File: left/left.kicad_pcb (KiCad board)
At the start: 2 copper layers, 173.8 x 173.8 mm, 67 parts, among them J1 HDMI_C_1.4, U1 Raspberry_Pi_Pico

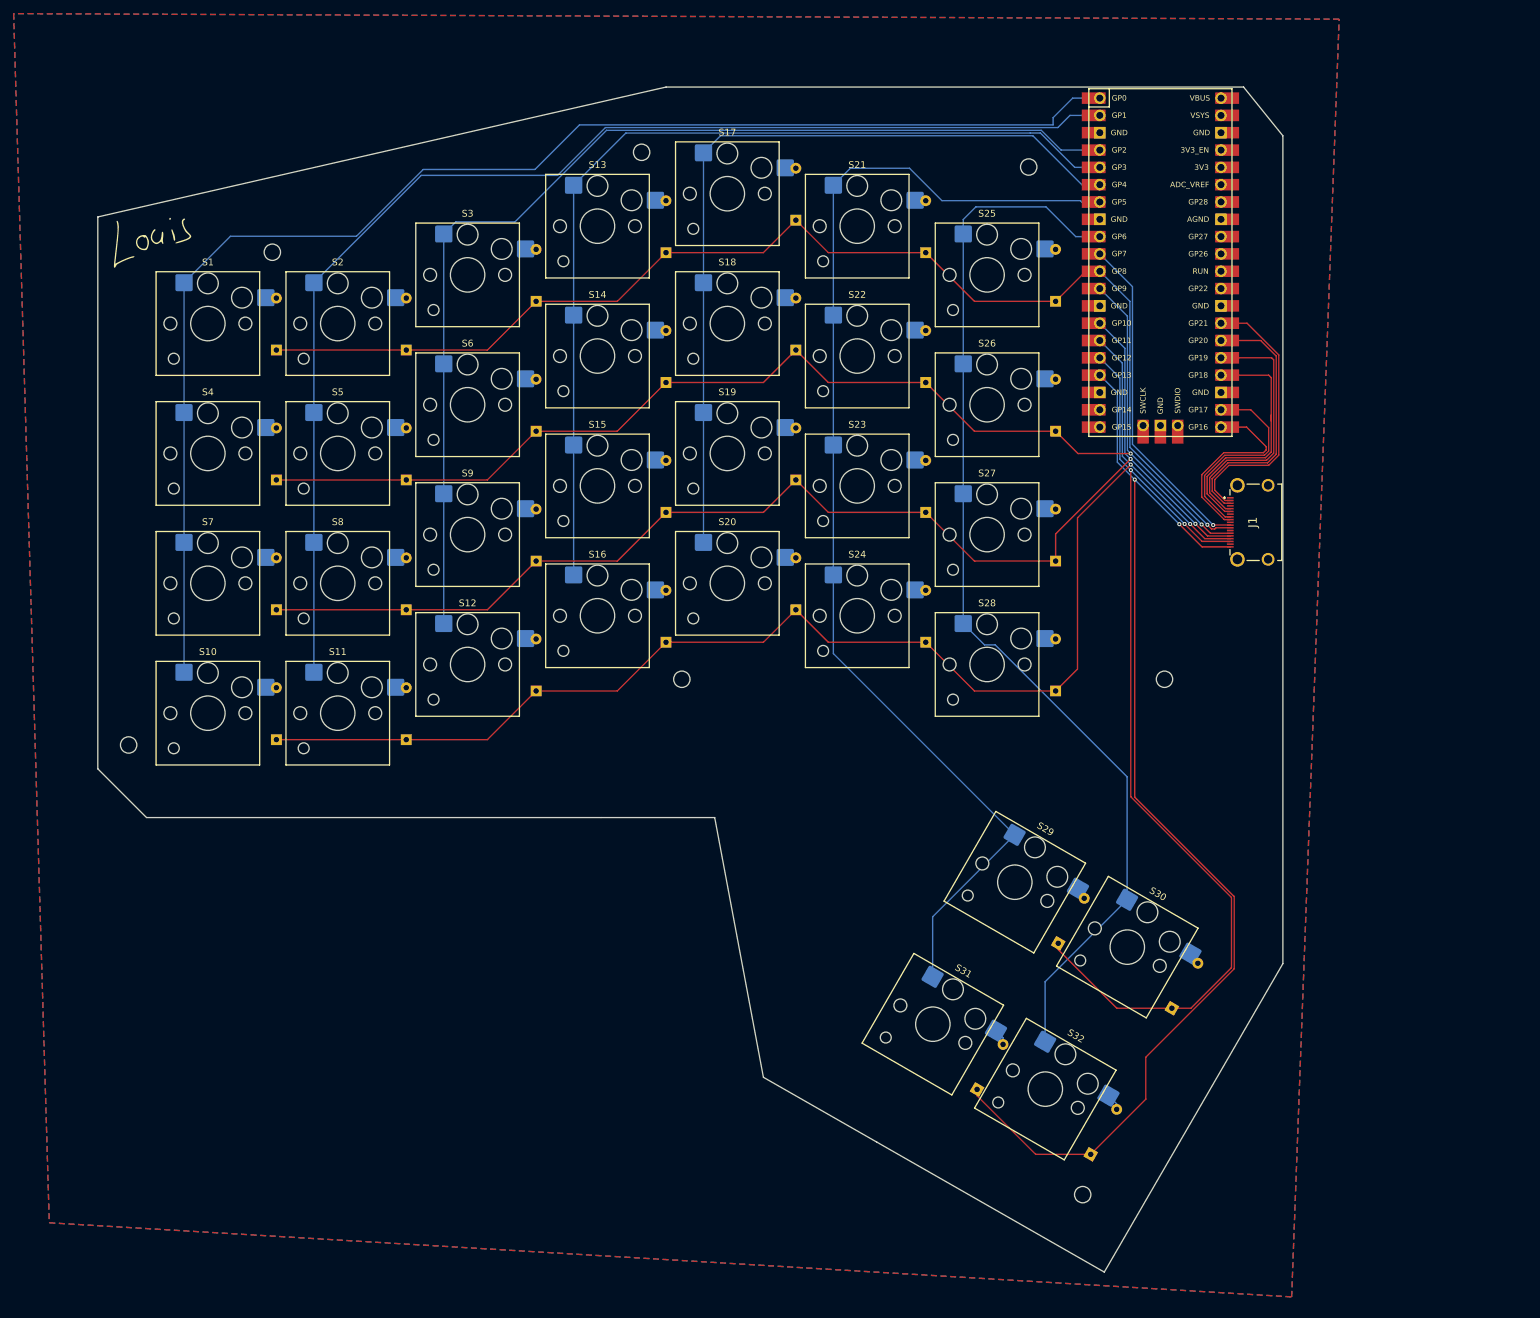
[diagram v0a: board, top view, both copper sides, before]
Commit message: Fix issues from update to KiCad 9
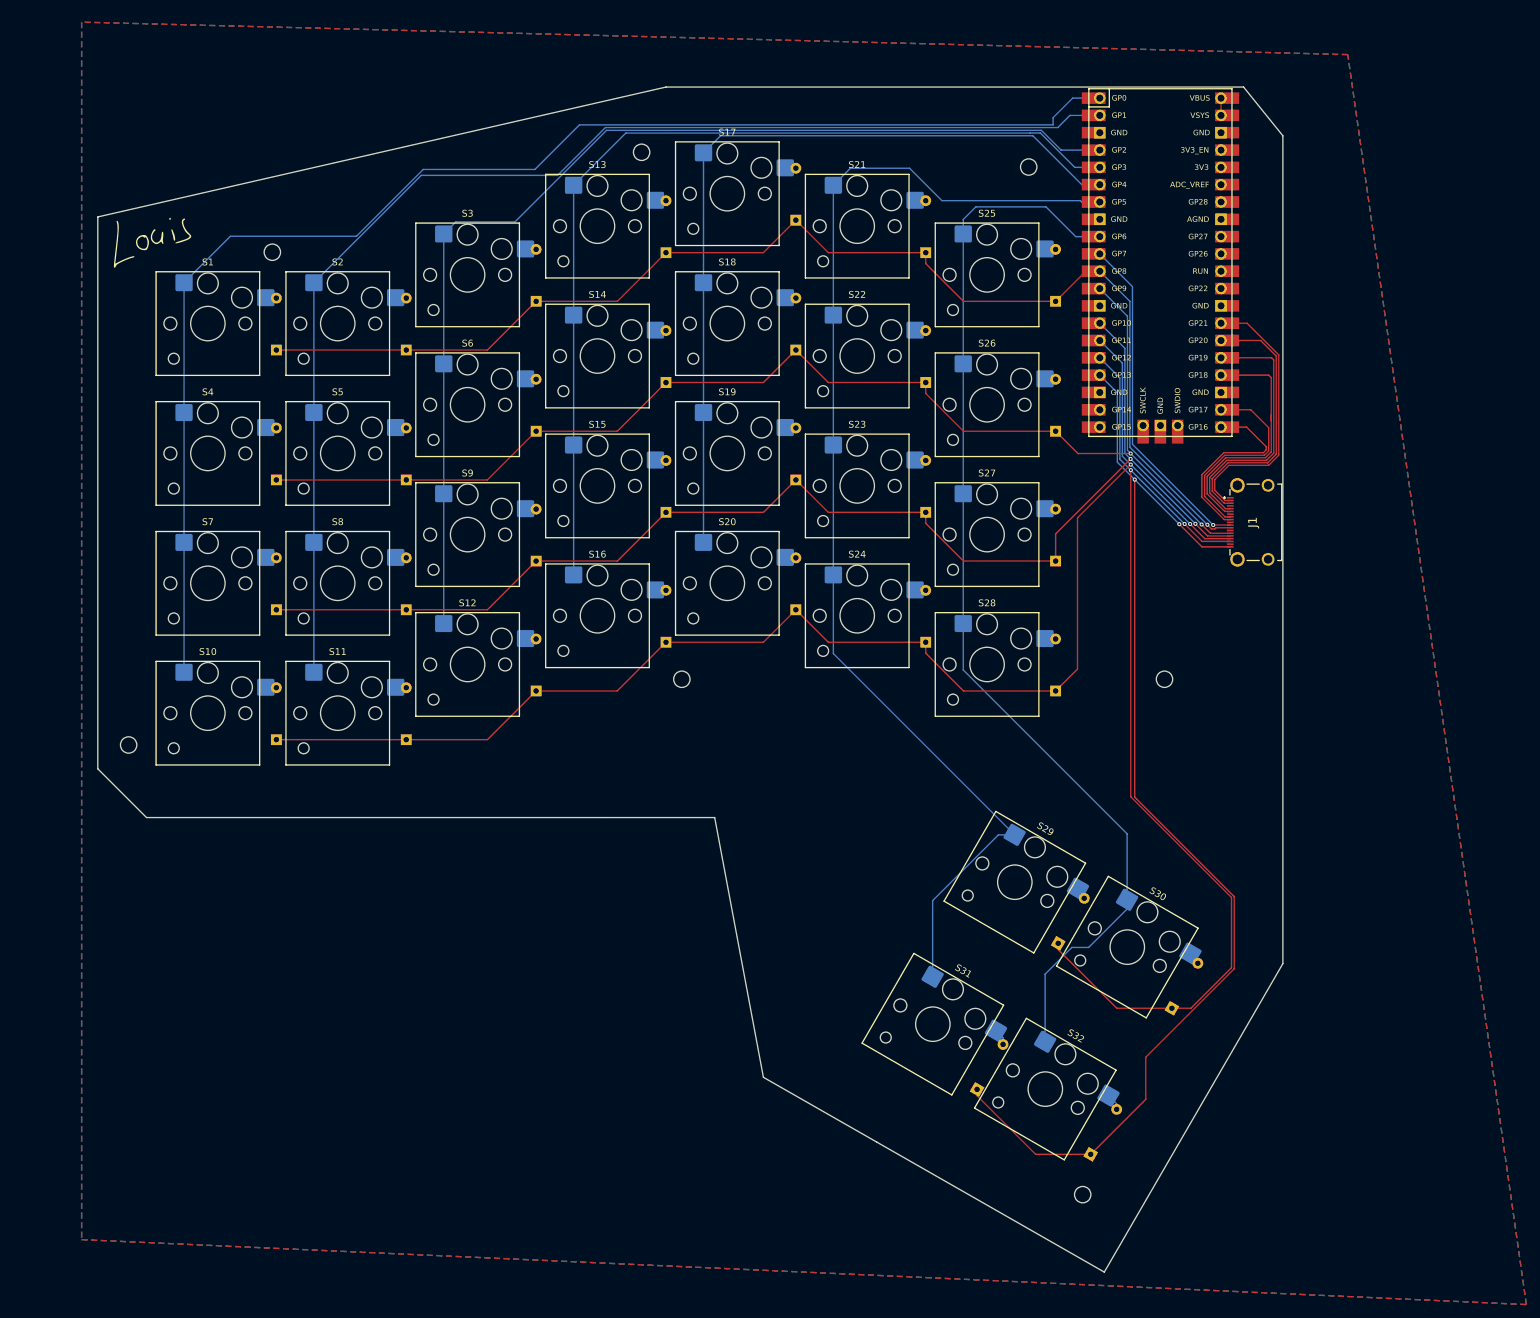
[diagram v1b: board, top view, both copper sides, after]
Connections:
- D10 pad 1: Row 1 -> Row 3
- D11 pad 1: Row 2 -> Row 3
- D2 pad 1: Row 1 -> Row 0
- D3 pad 1: Row 2 -> Row 0
- D30 pad 1: Row 5 -> Row 4
- D31 pad 1: Row 4 -> Row 5
- D4 pad 1: Row 3 -> Row 1
- D5 pad 1: Row 0 -> Row 1
- D8 pad 1: Row 3 -> Row 2
- D9 pad 1: Row 0 -> Row 2
- S10 pad 1: Col 2 -> Col 0
- S11 pad 1: Col 2 -> Col 1
- S2 pad 1: Col 0 -> Col 1
- S3 pad 1: Col 0 -> Col 2
- S30 pad 1: Col 5 -> Col 6
- S31 pad 1: Col 6 -> Col 5
- S6 pad 1: Col 1 -> Col 2
- S7 pad 1: Col 1 -> Col 0
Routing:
- net Net-(U1-VBUS): track 0.00 -> 2.54 mm
- net Col 5: track 174.3 -> 175.7 mm
- net Row 2: track 187.7 -> 188.7 mm
- net Row 3: track 204.1 -> 205.0 mm
- net Row 1: track 185.0 -> 186.0 mm
- net Row 0: track 182.6 -> 183.6 mm
- net Col 6: track 159.1 -> 159.6 mm

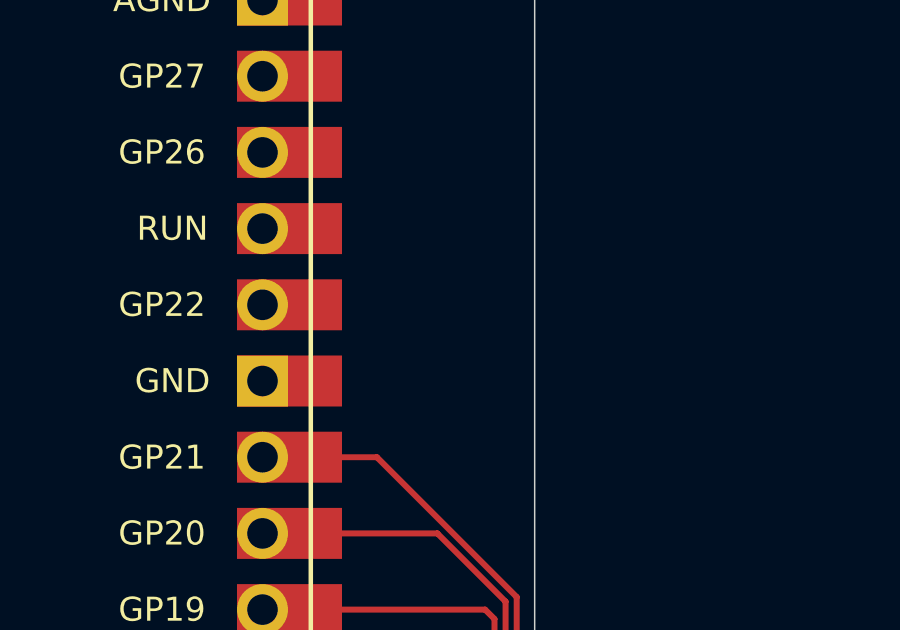
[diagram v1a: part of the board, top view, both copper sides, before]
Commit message: Add OSHW logo
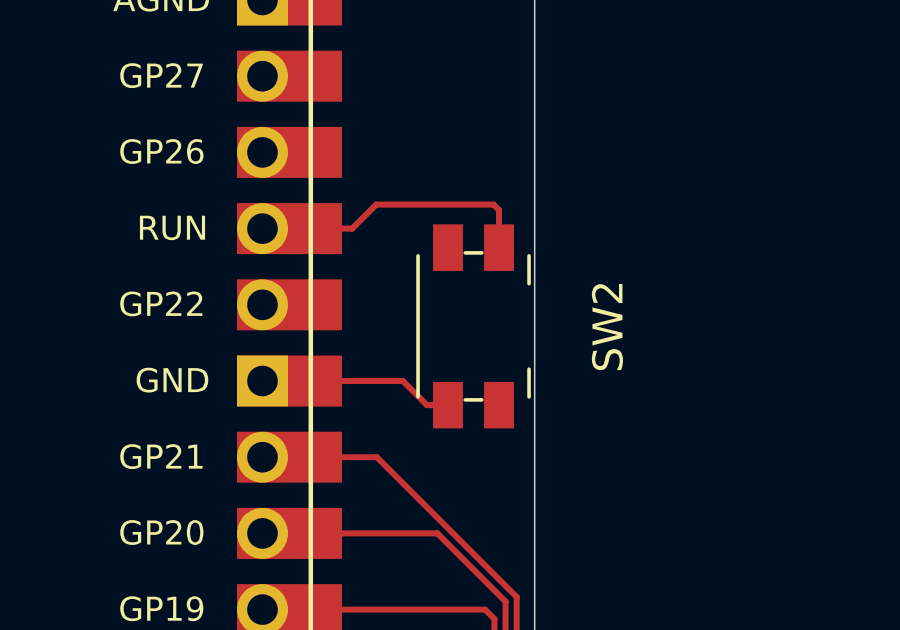
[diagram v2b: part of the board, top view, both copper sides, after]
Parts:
- added SW2: SW_Push, Button_Switch_SMD:Panasonic_EVQPUJ_EVQPUA, F.Cu at (231.3, 89.8)
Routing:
- net Net-(U1-RUN): track 0.00 -> 10.1 mm
- net Net-(SW2-Pad2): track 0.00 -> 6.52 mm
